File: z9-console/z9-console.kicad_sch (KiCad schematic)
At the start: 4 parts

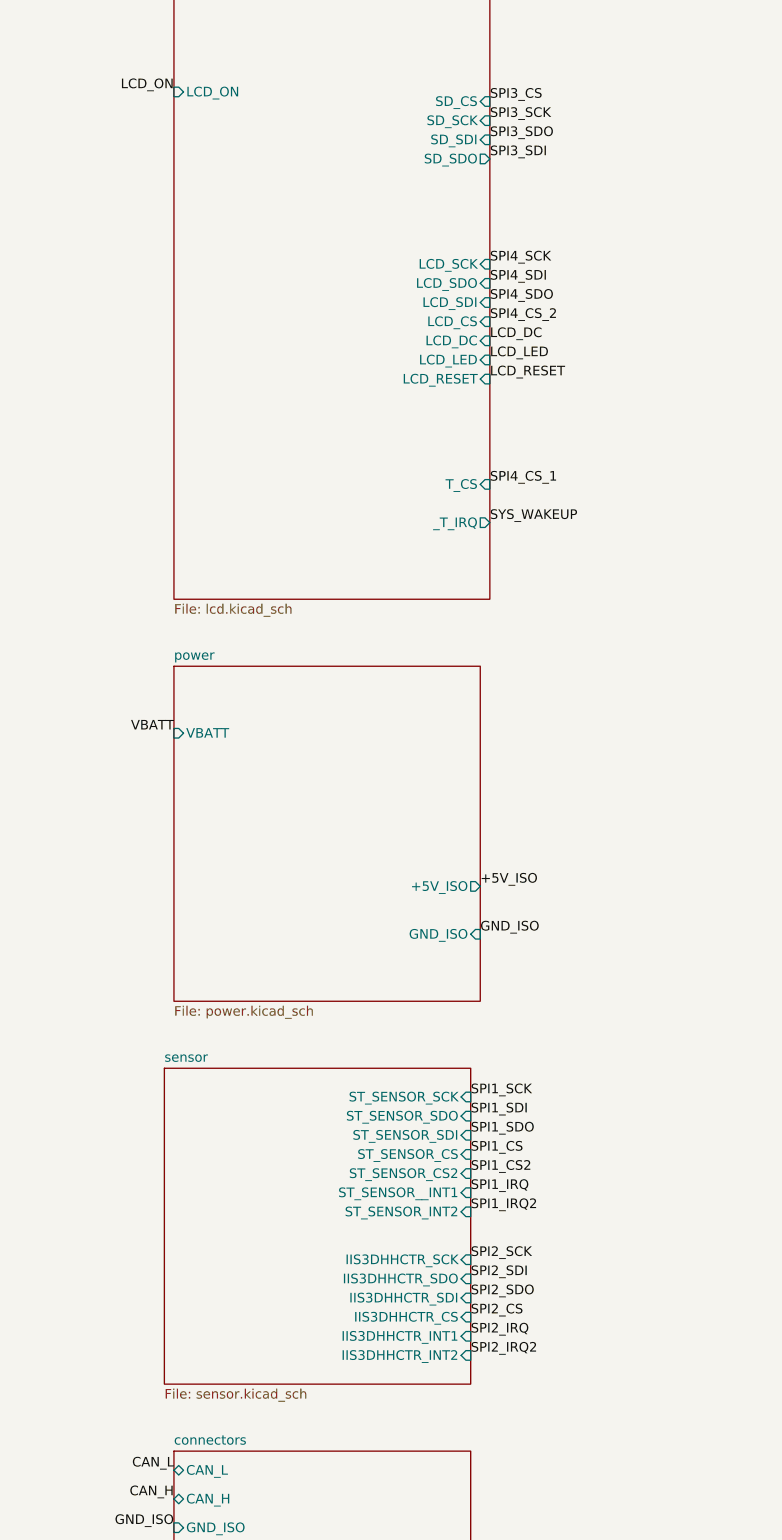
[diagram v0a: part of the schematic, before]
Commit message: fix stdc - reroute power on pcb
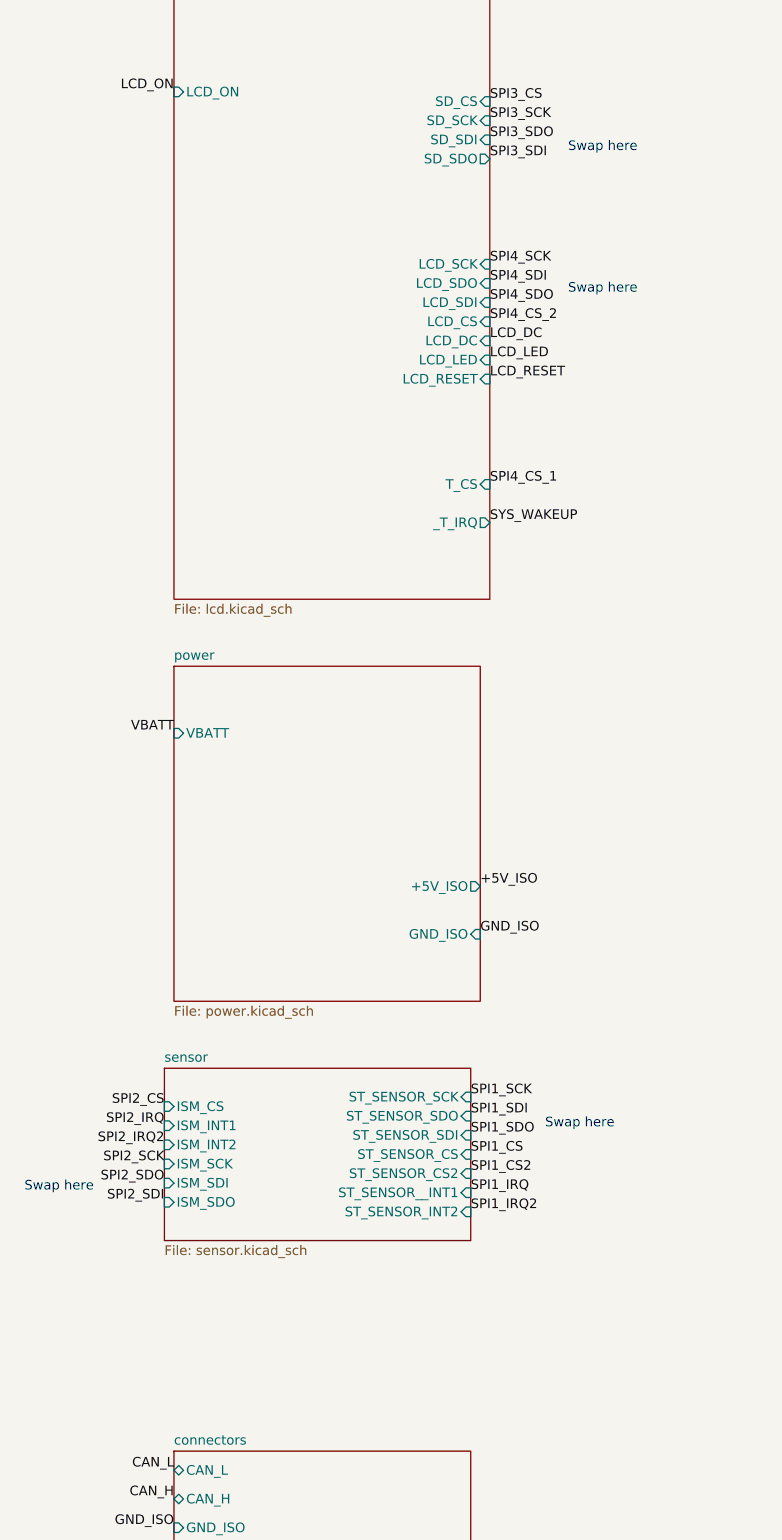
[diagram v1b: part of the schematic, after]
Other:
- sheet sensor ports: added ISM_CS, ISM_INT1, ISM_INT2, ISM_SCK, ISM_SDI, ISM_SDO; removed IIS3DHHCTR_CS, IIS3DHHCTR_INT1, IIS3DHHCTR_INT2, IIS3DHHCTR_SCK, IIS3DHHCTR_SDI, IIS3DHHCTR_SDO
- note added: "Swap here"
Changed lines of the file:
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@@
+		)
+	)
+	(text "Swap here"
+		(exclude_from_sim no)
+		(at 110.236 69.342 0)
+		(effects
+			(font
+				(size 1.27 1.27)
+			)
 		)
 	)
@@
 		)
 	)
+	(text "Swap here"
+		(exclude_from_sim no)
+		(at 110.236 50.546 0)
+		(effects
+			(font
+				(size 1.27 1.27)
+			)
+		)
+	)
+	(text "Swap here"
+		(exclude_from_sim no)
+		(at 107.188 180.086 0)
+		(effects
+			(font
+				(size 1.27 1.27)
+			)
+		)
+	)
+	(text "Swap here"
+		(exclude_from_sim no)
+		(at 38.1 188.468 0)
+		(effects
+			(font
+				(size 1.27 1.27)
+			)
+		)
+	)
 	(text "LCD/TOUCH"
 		(exclude_from_sim no)
@@
 		)
 	)
+	(label "SPI2_SCK"
+		(at 52.07 185.42 180)
+		(effects
+			(font
+				(size 1.27 1.27)
+			)
+			(justify right bottom)
+		)
+	)
 	(label "SPI1_IRQ"
 		(at 92.71 189.23 0)
@@
 		)
 	)
+	(label "SPI2_SDO"
+		(at 52.07 187.96 180)
+		(effects
+			(font
+				(size 1.27 1.27)
+			)
+			(justify right bottom)
+		)
+	)
 	(label "SPI4_SDI"
 		(at 222.25 205.74 0)
@@
 		)
 	)
-	(label "SPI2_SDO"
-		(at 92.71 203.2 0)
-		(effects
-			(font
-				(size 1.27 1.27)
-			)
-			(justify left bottom)
-		)
-	)
 	(label "SPI4_CS_2"
 		(at 95.25 73.66 0)
@@
 		)
 	)
+	(label "SPI2_CS"
+		(at 52.07 177.8 180)
+		(effects
+			(font
+				(size 1.27 1.27)
+			)
+			(justify right bottom)
+		)
+	)
 	(label "LCD_LED"
 		(at 222.25 229.87 0)
@@
 		)
 	)
-	(label "SPI2_IRQ"
-		(at 92.71 208.28 0)
-		(effects
-			(font
-				(size 1.27 1.27)
-			)
-			(justify left bottom)
-		)
-	)
 	(label "SPI3_CS"
 		(at 95.25 44.45 0)
@@
 		)
 	)
+	(label "SPI2_IRQ"
+		(at 52.07 180.34 180)
+		(effects
+			(font
+				(size 1.27 1.27)
+			)
+			(justify right bottom)
+		)
+	)
 	(label "SPI2_SDO"
 		(at 212.09 151.13 0)
@@
 		)
 	)
-	(label "SPI2_CS"
-		(at 92.71 205.74 0)
-		(effects
-			(font
-				(size 1.27 1.27)
-			)
-			(justify left bottom)
-		)
-	)
-	(label "SPI2_SCK"
-		(at 92.71 198.12 0)
-		(effects
-			(font
-				(size 1.27 1.27)
-			)
-			(justify left bottom)
-		)
-	)
 	(label "SPI2_SDI"
 		(at 212.09 153.67 0)
@@
 		)
 	)
+	(label "SPI2_IRQ2"
+		(at 52.07 182.88 180)
+		(effects
+			(font
+				(size 1.27 1.27)
+			)
+			(justify right bottom)
+		)
+	)
 	(label "SPI4_SCK"
 		(at 95.25 66.04 0)
@@
 		)
 	)
+	(label "SPI2_SDI"
+		(at 52.07 190.5 180)
+		(effects
+			(font
+				(size 1.27 1.27)
+			)
+			(justify right bottom)
+		)
+	)
 	(label "LCD_ON"
 		(at 53.34 43.18 180)
@@
 		)
 	)
-	(label "SPI2_SDI"
-		(at 92.71 200.66 0)
-		(effects
-			(font
-				(size 1.27 1.27)
-			)
-			(justify left bottom)
-		)
-	)
 	(label "SPI1_CS2"
 		(at 92.71 186.69 0)
@@
 	(label "SPI4_CS_2"
 		(at 222.25 215.9 0)
-		(effects
-			(font
-				(size 1.27 1.27)
-			)
-			(justify left bottom)
-		)
-	)
-	(label "SPI2_IRQ2"
-		(at 92.71 210.82 0)
 		(effects
 			(font
@@
 	(sheet
 		(at 52.07 172.72)
-		(size 40.64 41.91)
+		(size 40.64 22.86)
 		(exclude_from_sim no)
 		(in_bom yes)
@@
 		)
 		(property "Sheetfile" "sensor.kicad_sch"
-			(at 52.07 215.2146 0)
+			(at 52.07 196.1646 0)
 			(effects
 				(font
@@
 				)
 				(justify left top)
-			)
-		)
-		(pin "IIS3DHHCTR_INT2" input
-			(at 92.71 210.82 0)
-			(effects
-				(font
-					(size 1.27 1.27)
-				)
-				(justify right)
-			)
-		)
-		(pin "IIS3DHHCTR_INT1" input
-			(at 92.71 208.28 0)
-			(effects
-				(font
-					(size 1.27 1.27)
-				)
-				(justify right)
 			)
 		)
@@
 			)
 		)
-		(pin "IIS3DHHCTR_SDO" input
-			(at 92.71 200.66 0)
-			(effects
-				(font
-					(size 1.27 1.27)
-				)
-				(justify right)
-			)
-		)
-		(pin "IIS3DHHCTR_CS" input
-			(at 92.71 205.74 0)
-			(effects
-				(font
-					(size 1.27 1.27)
-				)
-				(justify right)
-			)
-		)
-		(pin "IIS3DHHCTR_SDI" input
-			(at 92.71 203.2 0)
-			(effects
-				(font
-					(size 1.27 1.27)
-				)
-				(justify right)
-			)
-		)
 		(pin "ST_SENSOR_CS" input
 			(at 92.71 184.15 0)
@@
 			)
 		)
-		(pin "IIS3DHHCTR_SCK" input
-			(at 92.71 198.12 0)
-			(effects
-				(font
-					(size 1.27 1.27)
-				)
-				(justify right)
-			)
-		)
+		(pin "ISM_CS" input
+			(at 52.07 177.8 180)
+			(effects
+				(font
+					(size 1.27 1.27)
+				)
+				(justify left)
+			)
+		)
+		(pin "ISM_INT1" input
+			(at 52.07 180.34 180)
+			(effects
+				(font
+					(size 1.27 1.27)
+				)
+				(justify left)
+			)
+		)
+		(pin "ISM_INT2" input
+			(at 52.07 182.88 180)
+			(effects
+				(font
+					(size 1.27 1.27)
+				)
+				(justify left)
+			)
+		)
+		(pin "ISM_SCK" input
+			(at 52.07 185.42 180)
+			(effects
+				(font
+					(size 1.27 1.27)
+				)
+				(justify left)
+			)
+		)
+		(pin "ISM_SDI" input
+			(at 52.07 187.96 180)
+			(effects
+				(font
+					(size 1.27 1.27)
+				)
+				(justify left)
+			)
+		)
+		(pin "ISM_SDO" input
+			(at 52.07 190.5 180)
+			(effects
+				(font
+					(size 1.27 1.27)
+				)
+				(justify left)
+			)
+		)
